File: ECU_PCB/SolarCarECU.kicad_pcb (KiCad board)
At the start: 4 copper layers, 160 x 100 mm, 151 parts, among them J2 Screw_Terminal_01x08, J3 Screw_Terminal_01x08, J4 Screw_Terminal_01x08, J5 Screw_Terminal_01x08, J6 Screw_Terminal_01x08, J7 Screw_Terminal_01x08, J8 Screw_Terminal_01x08, Q1 QM6015D, Q2 QM6015D, Q3 QM6015D, Q4 QM6015D, Q5 QM6015D, Q6 QM6015D, Q7 QM6015D, U1 Teensy3.6, U10 LM324A, U11 MCP1403, U2 MCP1403, U3 MCP1403, U4 L7805, U5 MCP2562-E-P, U6 MCP2562-E-P, U7 4504, U8 4504, U9 4504

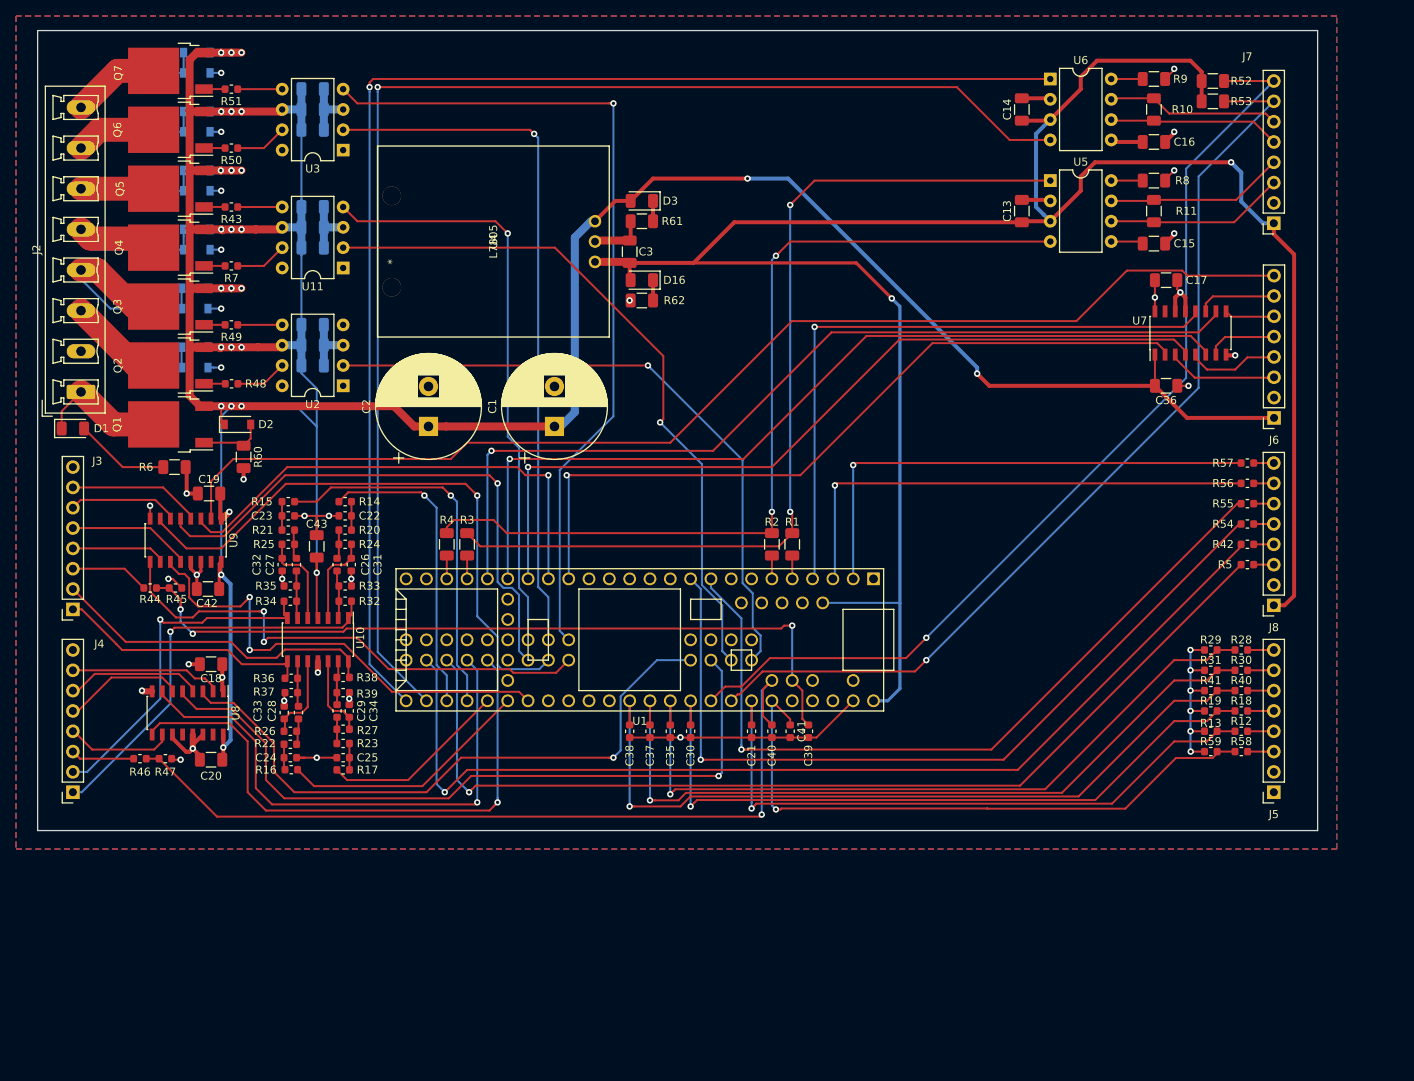
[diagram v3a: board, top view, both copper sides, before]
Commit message: added HORN_CTRL and fixed silkscreen issues
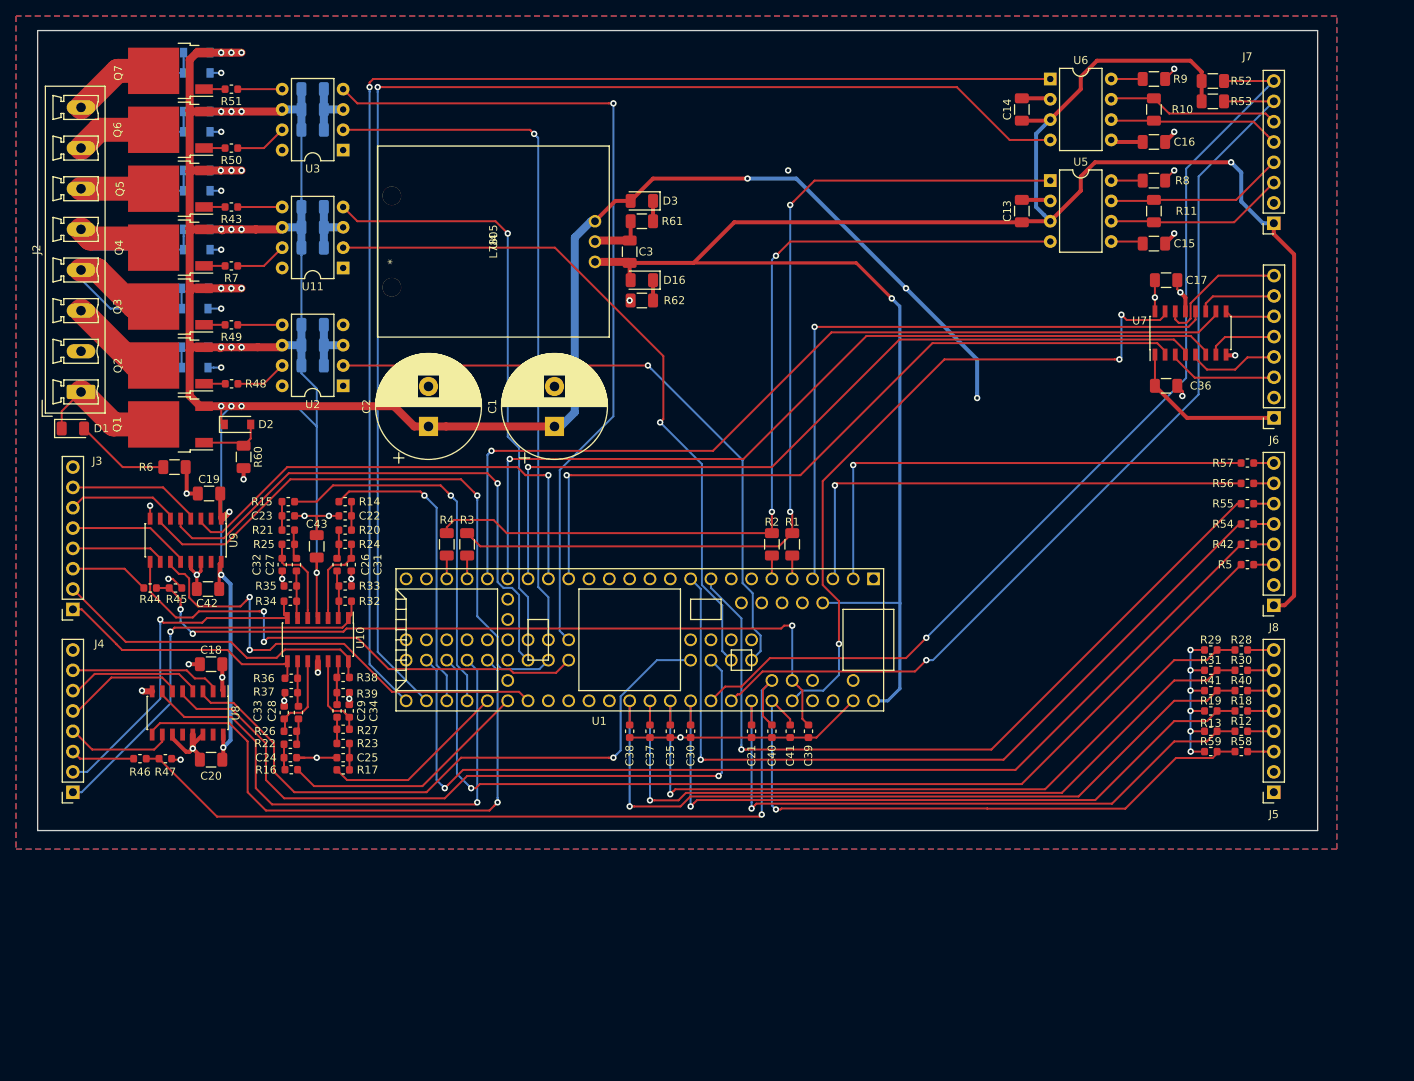
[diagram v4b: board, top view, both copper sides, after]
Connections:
- J6 pad 8: /HAZARD_LED -> /HORN_CTRL
- U1 pad 49: Net-(U1-Pad49) -> /LV_HORN_CTRL
- U7 pad 14: GND -> /HORN_CTRL
- U7 pad 15: Net-(U7-Pad15) -> /LV_HORN_CTRL
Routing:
- net /HAZARD_LED: track 149.2 -> 0.45 mm
- net /LV_HORN_CTRL: track 0.00 -> 87.8 mm, vias 0 -> 3
- net +12V: track 429.0 -> 409.8 mm, vias 26 -> 28
- net /HORN_CTRL: track 0.00 -> 17.1 mm
- net GND: track 89.1 -> 86.7 mm
- net /UART_6_RX: track 130.0 -> 129.1 mm
- net /UART_6_TX: track 125.9 -> 125.1 mm

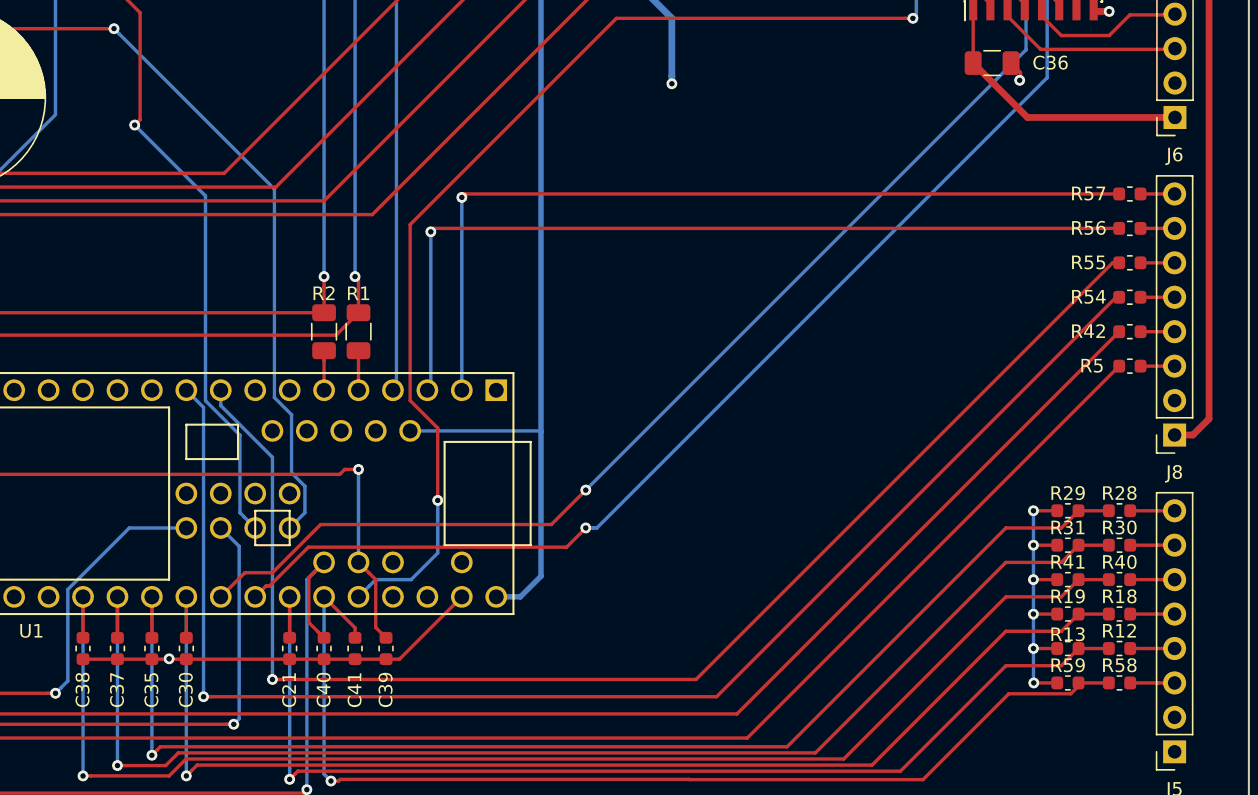
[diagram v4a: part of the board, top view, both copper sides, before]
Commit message: added HEADLIGHT_CTRL pin but had to sacrifice a 12V output for it.
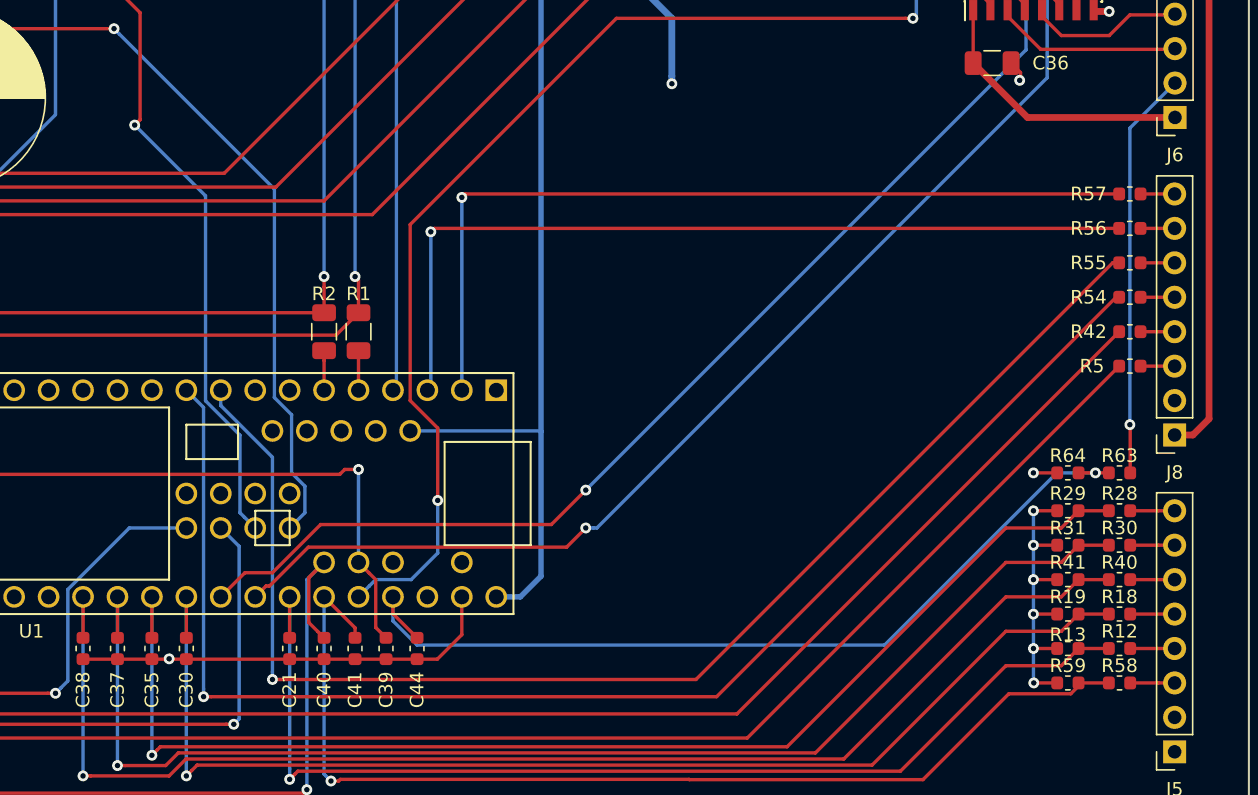
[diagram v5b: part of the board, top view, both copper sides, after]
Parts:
- added C44: 1n, Capacitor_SMD:C_0603_1608Metric, F.Cu at (175.3, 104.6)
- added R63: 1M, Resistor_SMD:R_0603_1608Metric, F.Cu at (227.1, 91.7)
- added R64: 330k, Resistor_SMD:R_0603_1608Metric, F.Cu at (223.3, 91.7)
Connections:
- J6 pad 1: +12V -> GNDA
- J6 pad 2: GNDA -> /HEADLIGHT_CTRL
- U1 pad 50: Net-(U1-Pad50) -> /LV_HEADLIGHT_CTRL
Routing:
- net /LV_HEADLIGHT_CTRL: track 0.00 -> 65.6 mm, vias 0 -> 1
- net /HEADLIGHT_CTRL: track 0.00 -> 30.1 mm, vias 0 -> 1
- net GNDA: track 78.0 -> 81.4 mm, vias 16 -> 17

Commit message: fixed PCB and schematic
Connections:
- U1 pad 8: Net-(U1-Pad8) -> /LV_STROBE
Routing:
- net /LV_STROBE: track 0.00 -> 71.0 mm, vias 0 -> 1
- net +12V: track 409.8 -> 393.3 mm
- net /LV_MOTOR_L_REV_EN: track 79.3 -> 80.4 mm
